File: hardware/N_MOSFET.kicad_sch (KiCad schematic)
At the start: 4 parts, among them Q4 Q_NMOS_DGS

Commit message: minor improvements
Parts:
- renumbered Q4 to Q5, R31 to R34, R32 to R35, R33 to R36
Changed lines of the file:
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@@
   (symbol (lib_id "Device:Q_NMOS_DGS") (at 161.29 102.87 0)
     (in_bom yes) (on_board yes)
-    (property "Reference" "Q4" (id 0) (at 170.18 104.14 90)
+    (property "Reference" "Q5" (id 0) (at 170.18 104.14 90)
       (effects (font (size 1.27 1.27)) (justify left))
     )
@@
   (symbol (lib_id "Device:R_Small") (at 153.67 107.95 0) (mirror y)
     (in_bom yes) (on_board yes)
-    (property "Reference" "R32" (id 0) (at 151.13 107.95 90)
+    (property "Reference" "R35" (id 0) (at 151.13 107.95 90)
       (effects (font (size 1.27 1.27)) (justify left))
     )
@@
   (symbol (lib_id "Device:R_Small") (at 148.59 102.87 90) (mirror x)
     (in_bom yes) (on_board yes)
-    (property "Reference" "R31" (id 0) (at 148.59 105.41 90)
+    (property "Reference" "R34" (id 0) (at 148.59 105.41 90)
       (effects (font (size 1.27 1.27)) (justify left))
     )
@@
   (symbol (lib_id "Device:R_Small") (at 163.83 92.71 0) (mirror y)
     (in_bom yes) (on_board yes)
-    (property "Reference" "R33" (id 0) (at 161.29 92.71 90)
+    (property "Reference" "R36" (id 0) (at 161.29 92.71 90)
       (effects (font (size 1.27 1.27)) (justify left))
     )

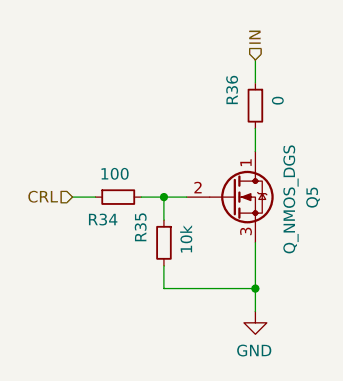
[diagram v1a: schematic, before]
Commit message: added traceswo from pin 55 to progrmator
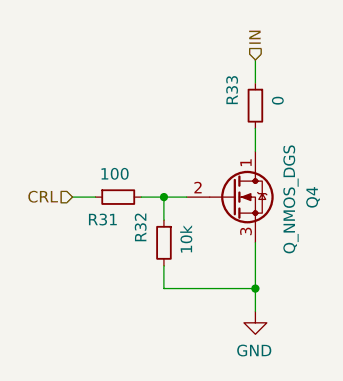
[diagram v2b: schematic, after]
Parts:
- renumbered Q5 to Q4, R34 to R31, R35 to R32, R36 to R33
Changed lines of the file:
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@@
   (symbol (lib_id "Device:Q_NMOS_DGS") (at 161.29 102.87 0)
     (in_bom yes) (on_board yes)
-    (property "Reference" "Q5" (id 0) (at 170.18 104.14 90)
+    (property "Reference" "Q4" (id 0) (at 170.18 104.14 90)
       (effects (font (size 1.27 1.27)) (justify left))
     )
@@
   (symbol (lib_id "Device:R_Small") (at 153.67 107.95 0) (mirror y)
     (in_bom yes) (on_board yes)
-    (property "Reference" "R35" (id 0) (at 151.13 107.95 90)
+    (property "Reference" "R32" (id 0) (at 151.13 107.95 90)
       (effects (font (size 1.27 1.27)) (justify left))
     )
@@
   (symbol (lib_id "Device:R_Small") (at 148.59 102.87 90) (mirror x)
     (in_bom yes) (on_board yes)
-    (property "Reference" "R34" (id 0) (at 148.59 105.41 90)
+    (property "Reference" "R31" (id 0) (at 148.59 105.41 90)
       (effects (font (size 1.27 1.27)) (justify left))
     )
@@
   (symbol (lib_id "Device:R_Small") (at 163.83 92.71 0) (mirror y)
     (in_bom yes) (on_board yes)
-    (property "Reference" "R36" (id 0) (at 161.29 92.71 90)
+    (property "Reference" "R33" (id 0) (at 161.29 92.71 90)
       (effects (font (size 1.27 1.27)) (justify left))
     )
@@
   (symbol (lib_id "power:GND") (at 163.83 115.57 0) (mirror y)
     (in_bom yes) (on_board yes)
-    (property "Reference" "#PWR0107" (id 0) (at 163.83 121.92 0)
+    (property "Reference" "#PWR0125" (id 0) (at 163.83 121.92 0)
       (effects (font (size 1.27 1.27)) hide)
     )

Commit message: fuck
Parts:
- renumbered Q4 to Q1, R31 to R21, R32 to R22, R33 to R23
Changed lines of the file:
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@@
   (symbol (lib_id "Device:Q_NMOS_DGS") (at 161.29 102.87 0)
     (in_bom yes) (on_board yes)
-    (property "Reference" "Q4" (id 0) (at 170.18 104.14 90)
+    (property "Reference" "Q1" (id 0) (at 170.18 104.14 90)
       (effects (font (size 1.27 1.27)) (justify left))
     )
@@
   (symbol (lib_id "Device:R_Small") (at 153.67 107.95 0) (mirror y)
     (in_bom yes) (on_board yes)
-    (property "Reference" "R32" (id 0) (at 151.13 107.95 90)
+    (property "Reference" "R22" (id 0) (at 151.13 107.95 90)
       (effects (font (size 1.27 1.27)) (justify left))
     )
@@
   (symbol (lib_id "Device:R_Small") (at 148.59 102.87 90) (mirror x)
     (in_bom yes) (on_board yes)
-    (property "Reference" "R31" (id 0) (at 148.59 105.41 90)
+    (property "Reference" "R21" (id 0) (at 148.59 105.41 90)
       (effects (font (size 1.27 1.27)) (justify left))
     )
@@
   (symbol (lib_id "Device:R_Small") (at 163.83 92.71 0) (mirror y)
     (in_bom yes) (on_board yes)
-    (property "Reference" "R33" (id 0) (at 161.29 92.71 90)
+    (property "Reference" "R23" (id 0) (at 161.29 92.71 90)
       (effects (font (size 1.27 1.27)) (justify left))
     )
@@
   (symbol (lib_id "power:GND") (at 163.83 115.57 0) (mirror y)
     (in_bom yes) (on_board yes)
-    (property "Reference" "#PWR0125" (id 0) (at 163.83 121.92 0)
+    (property "Reference" "#PWR0106" (id 0) (at 163.83 121.92 0)
       (effects (font (size 1.27 1.27)) hide)
     )

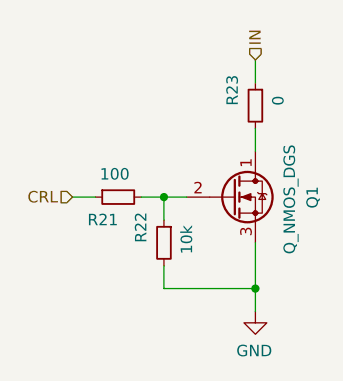
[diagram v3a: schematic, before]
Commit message: changed clock and 5v converter coils, footprints rearrange commponets to fit the need now the board connector is vertical not horizontal relative to the pcb's longest side
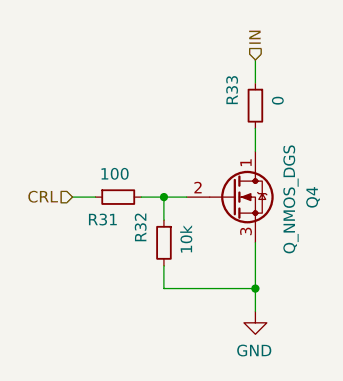
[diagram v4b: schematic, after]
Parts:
- renumbered Q1 to Q4, R21 to R31, R22 to R32, R23 to R33
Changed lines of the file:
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@@
   (symbol (lib_id "Device:Q_NMOS_DGS") (at 161.29 102.87 0)
     (in_bom yes) (on_board yes)
-    (property "Reference" "Q1" (id 0) (at 170.18 104.14 90)
+    (property "Reference" "Q4" (id 0) (at 170.18 104.14 90)
       (effects (font (size 1.27 1.27)) (justify left))
     )
@@
   (symbol (lib_id "Device:R_Small") (at 153.67 107.95 0) (mirror y)
     (in_bom yes) (on_board yes)
-    (property "Reference" "R22" (id 0) (at 151.13 107.95 90)
+    (property "Reference" "R32" (id 0) (at 151.13 107.95 90)
       (effects (font (size 1.27 1.27)) (justify left))
     )
@@
   (symbol (lib_id "Device:R_Small") (at 148.59 102.87 90) (mirror x)
     (in_bom yes) (on_board yes)
-    (property "Reference" "R21" (id 0) (at 148.59 105.41 90)
+    (property "Reference" "R31" (id 0) (at 148.59 105.41 90)
       (effects (font (size 1.27 1.27)) (justify left))
     )
@@
   (symbol (lib_id "Device:R_Small") (at 163.83 92.71 0) (mirror y)
     (in_bom yes) (on_board yes)
-    (property "Reference" "R23" (id 0) (at 161.29 92.71 90)
+    (property "Reference" "R33" (id 0) (at 161.29 92.71 90)
       (effects (font (size 1.27 1.27)) (justify left))
     )
@@
   (symbol (lib_id "power:GND") (at 163.83 115.57 0) (mirror y)
     (in_bom yes) (on_board yes)
-    (property "Reference" "#PWR0106" (id 0) (at 163.83 121.92 0)
+    (property "Reference" "#PWR0107" (id 0) (at 163.83 121.92 0)
       (effects (font (size 1.27 1.27)) hide)
     )
